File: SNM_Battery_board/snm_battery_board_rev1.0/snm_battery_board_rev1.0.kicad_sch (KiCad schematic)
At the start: 26 parts, among them J1 Ext. SW_SPDT, J2 Conn_BAT, SW1 SW_SPDT, U1 BQ24075RGT, U2 TPS61220DCK

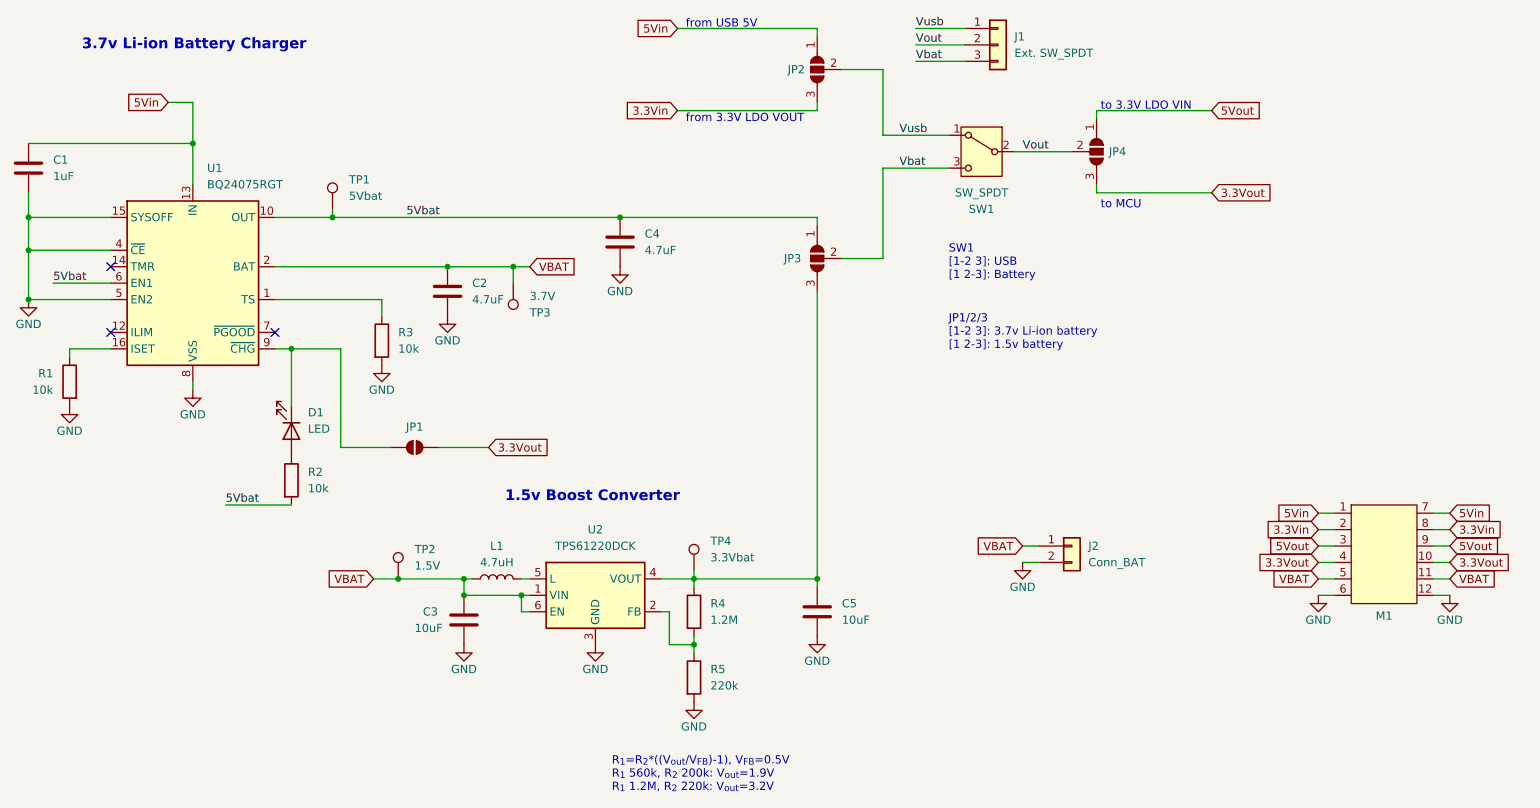
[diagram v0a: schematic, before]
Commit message: feat: add v4 battery & core board
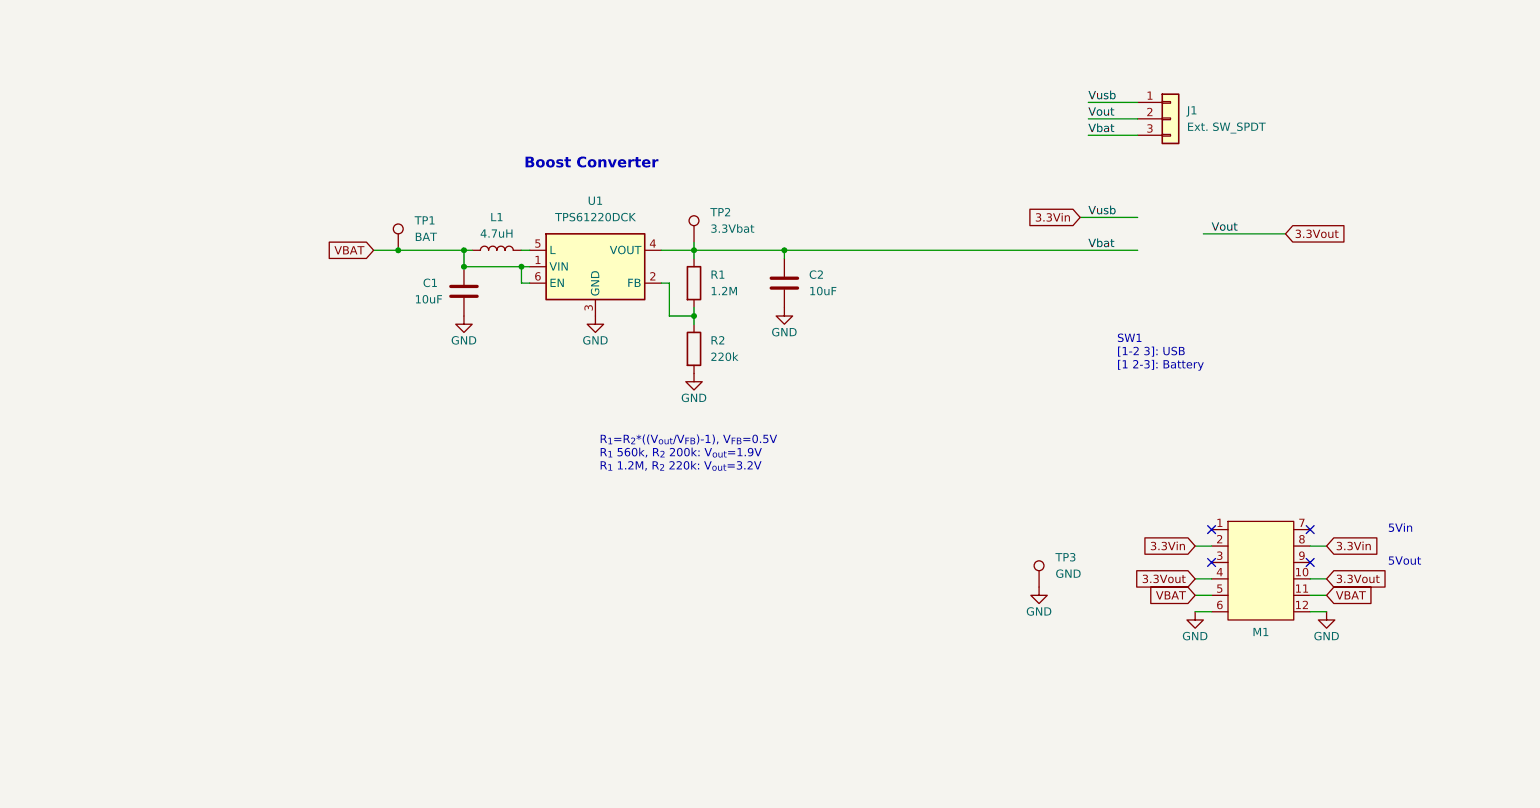
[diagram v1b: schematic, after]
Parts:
- removed C1: 1uF, Capacitor_SMD:C_0603_1608Metric, symbol Device:C
- removed C2, C4: 4.7uF, Capacitor_SMD:C_0603_1608Metric, symbol Device:C
- removed D1: LED, symbol Device:LED
- removed J2: Conn_BAT, symbol Connector_Generic:Conn_01x02
- removed JP1: SolderJumper_2_Open, symbol Jumper:SolderJumper_2_Open
- removed JP2, JP3, JP4: SolderJumper_3_Open, symbol Jumper:SolderJumper_3_Open
- removed R1, R2, R3: 10k, Resistor_SMD:R_0603_1608Metric, symbol Device:R
- removed SW1: SW_SPDT, symbol Switch:SW_SPDT
- removed TP1: 5Vbat, symbol Connector:TestPoint
- removed U1: BQ24075RGT, Package_DFN_QFN:VQFN-16-1EP_3x3mm_P0.5mm_EP1.6x1.6mm, symbol Battery_Management:BQ24075RGT
- J1: footprint (none) -> Connector_JST:JST_PH_S3B-PH-SM4-TB_1x03-1MP_P2.00mm_Horizontal
- TP1: renamed from TP2; value 1.5V -> BAT; footprint (none) -> TestPoint:TestPoint_Pad_D1.5mm
- TP2: renamed from TP4; footprint (none) -> TestPoint:TestPoint_Pad_D1.5mm
- TP3: value 3.7V -> GND; footprint (none) -> TestPoint:TestPoint_Pad_D1.5mm
- renumbered C3 to C1, C5 to C2, R4 to R1, R5 to R2, U2 to U1
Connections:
- net Vout is gone; now on net 3.3Vout: J1.2 (Pin_2)
- net Vusb is gone; now on net 3.3Vin: J1.1 (Pin_1)
- net GND: now also TP3.1
- net VBAT: no longer TP3.1
- net Vbat: now also C2.1, R1.1, TP2.1, U1.4 (VOUT)
- net 5Vin: no longer names the net of M1.1
- net 5Vin: no longer M1.7
- net 5Vout: no longer names the net of M1.3
- net 5Vout: no longer M1.9
- no-connect marks 3 -> 4
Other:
- note added: "5Vin"
- note added: "5Vout"
- note added: "Boost Converter"
- note removed: "1.5v Boost Converter"
- note removed: "3.7v Li-ion Battery Charger"
- note removed: "JP1/2/3 [1-2 3]: 3.7v Li-ion battery [1 2-3]: 1.5v battery"
- note removed: "from 3.3V LDO VOUT"
- note removed: "from USB 5V"
- note removed: "to 3.3V LDO VIN"
- note removed: "to MCU"
- moved on the sheet: C1, C2, J1, L1, M1, R1, R2, TP1, TP2, U1
